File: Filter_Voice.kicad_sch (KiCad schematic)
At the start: 28 parts, among them U3 TL074, U5 SSI2144

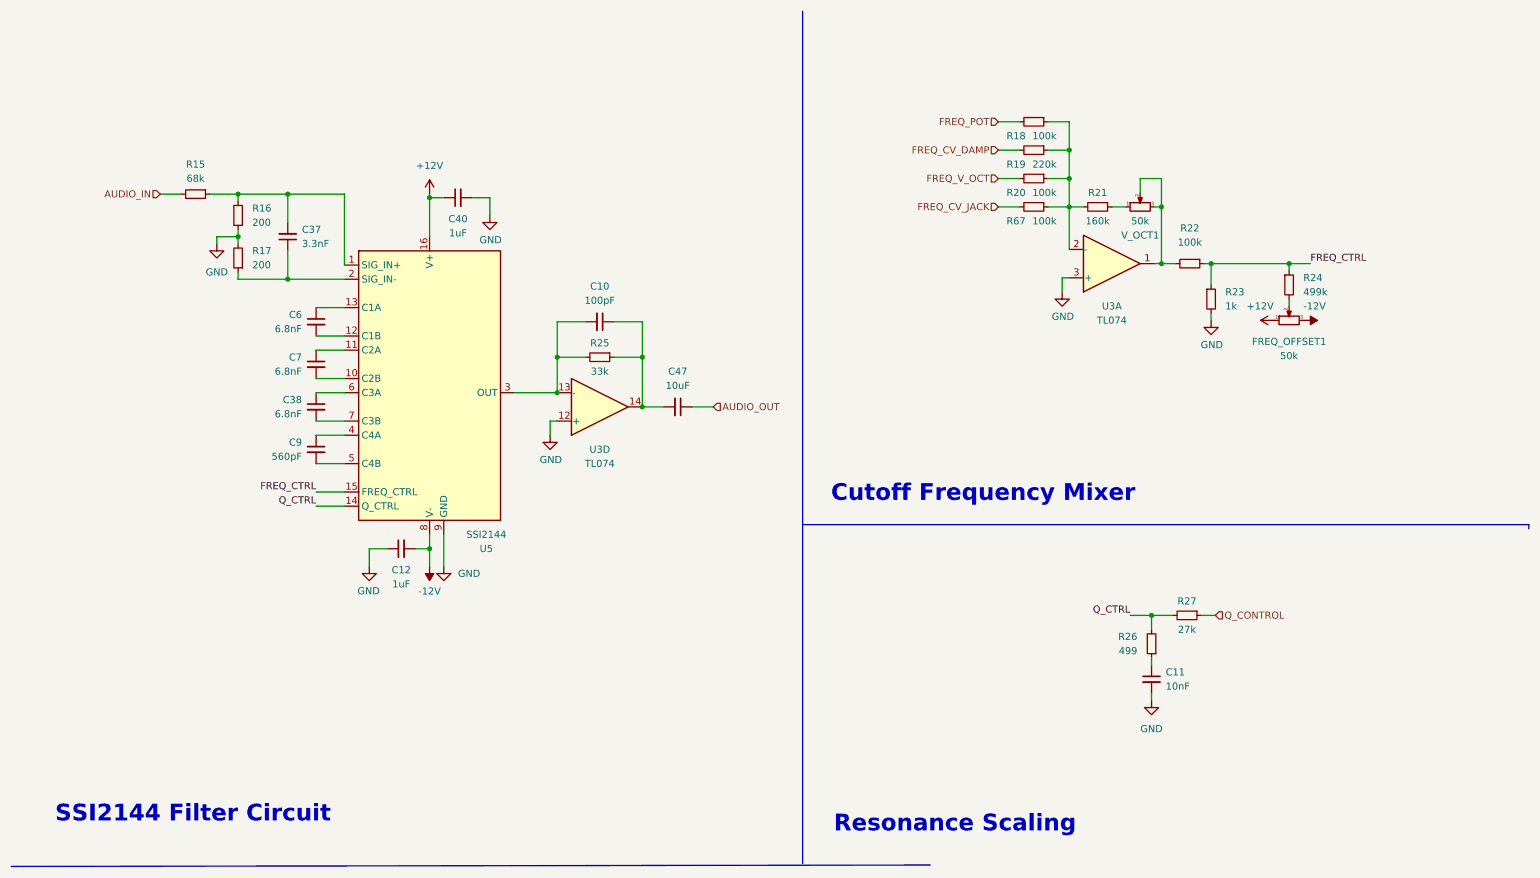
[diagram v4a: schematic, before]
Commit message: Updates for v2, including dc blocking caps on output
Also adjusted lower range of cutoff knob and tweaked various resistor values
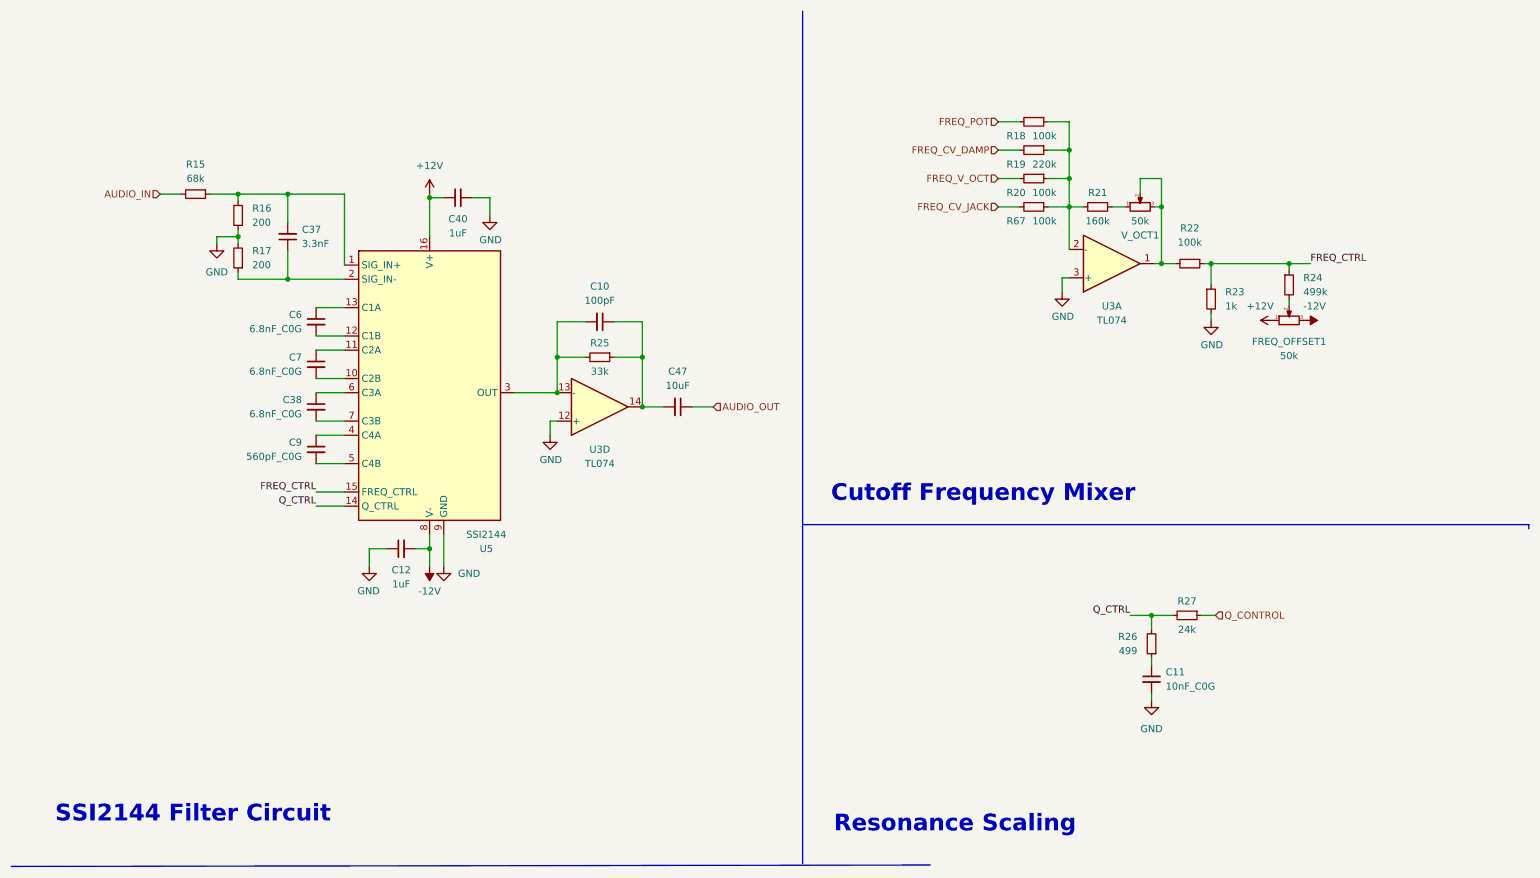
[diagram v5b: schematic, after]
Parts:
- C11: value 10nF -> 10nF_C0G
- C38, C6, C7: value 6.8nF -> 6.8nF_C0G
- C9: value 560pF -> 560pF_C0G
- R27: value 27k -> 24k
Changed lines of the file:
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@@
       (effects (font (size 1.27 1.27)) (justify right))
     )
-    (property "Value" "6.8nF" (id 1) (at 64.77 85.0962 0)
+    (property "Value" "6.8nF_C0G" (id 1) (at 64.77 85.0962 0)
       (effects (font (size 1.27 1.27)) (justify right))
     )
@@
       (effects (font (size 1.27 1.27)) (justify right))
     )
-    (property "Value" "6.8nF" (id 1) (at 64.77 77.4762 0)
+    (property "Value" "6.8nF_C0G" (id 1) (at 64.77 77.4762 0)
       (effects (font (size 1.27 1.27)) (justify right))
     )
@@
       (effects (font (size 1.27 1.27)) (justify right))
     )
-    (property "Value" "560pF" (id 1) (at 64.77 92.7162 0)
+    (property "Value" "560pF_C0G" (id 1) (at 64.77 92.7162 0)
       (effects (font (size 1.27 1.27)) (justify right))
     )
@@
   )
   (symbol (lib_id "Device:C_Small") (at 67.31 68.58 0) (unit 1)
-    (in_bom yes) (on_board yes) (fields_autoplaced)
+    (in_bom yes) (on_board yes)
     (property "Reference" "C6" (id 0) (at 64.77 67.3162 0)
       (effects (font (size 1.27 1.27)) (justify right))
     )
-    (property "Value" "6.8nF" (id 1) (at 64.77 69.8562 0)
+    (property "Value" "6.8nF_C0G" (id 1) (at 64.77 69.8562 0)
       (effects (font (size 1.27 1.27)) (justify right))
     )
@@
     (in_bom yes) (on_board yes)
     (property "Reference" "R27" (id 0) (at 223.266 118.618 90))
-    (property "Value" "27k" (id 1) (at 223.266 123.698 90))
+    (property "Value" "24k" (id 1) (at 223.266 123.698 90))
     (property "Footprint" "Resistor_SMD:R_0603_1608Metric_Pad0.98x0.95mm_HandSolder" (id 2) (at 223.266 121.158 0)
       (effects (font (size 1.27 1.27)) hide)
@@
       (effects (font (size 1.27 1.27)) (justify left))
     )
-    (property "Value" "10nF" (id 1) (at 219.456 133.8642 0)
-      (effects (font (size 1.27 1.27)) (justify left))
-    )
+    (property "Value" "10nF_C0G" (id 1) (at 219.456 133.8642 0)
+      (effects (font (size 1.27 1.27)) (justify left))
+    )

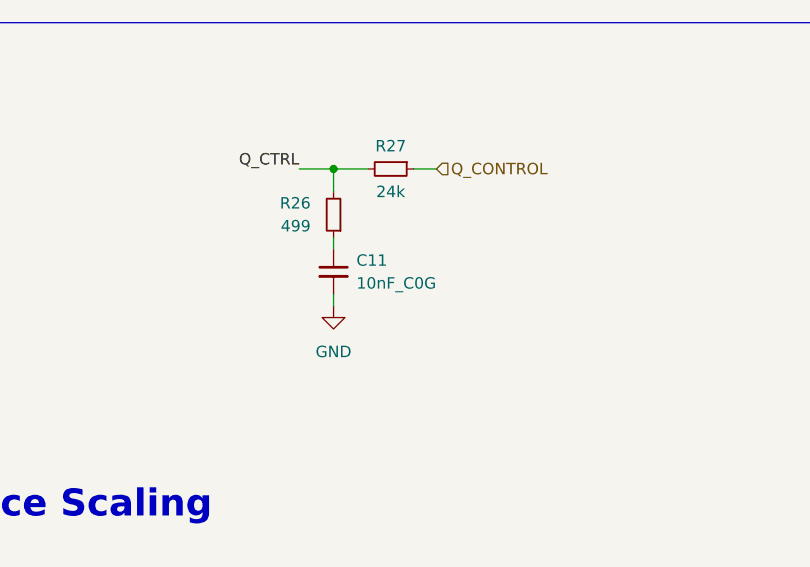
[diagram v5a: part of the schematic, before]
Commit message: Prepared v2 Controls and Components for manufacture
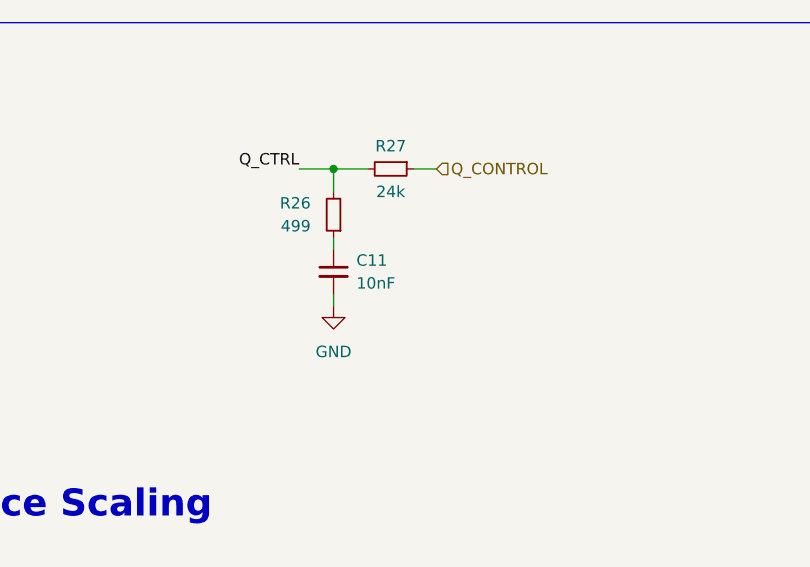
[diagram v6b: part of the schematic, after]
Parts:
- C11: value 10nF_C0G -> 10nF
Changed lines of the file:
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@@
       (effects (font (size 1.27 1.27)) (justify left))
     )
-    (property "Value" "10nF_C0G" (id 1) (at 219.456 133.8642 0)
+    (property "Value" "10nF" (id 1) (at 219.456 133.8642 0)
       (effects (font (size 1.27 1.27)) (justify left))
     )
